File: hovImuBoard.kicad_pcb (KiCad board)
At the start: 2 copper layers, 71 x 60 mm, 78 parts, among them J1 AVR-ISP-6, J2 Ext. Power, J3 54602-908LF, J4 AVR-JTAG-10, J5 ExtensionPort, U1 LD2981, U2 BMX160, U3 SN65HVD32DR, U4 ATmega1284P-AU, U5 TPS62173DSG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

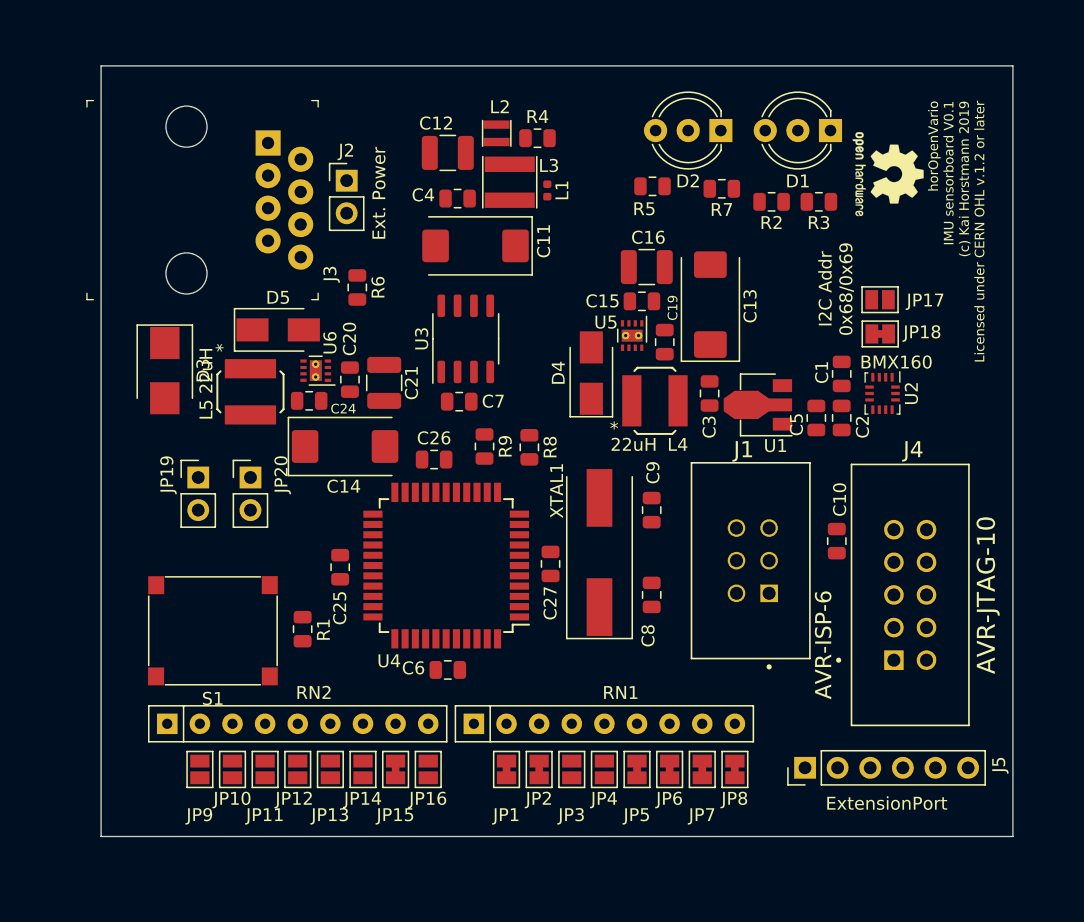
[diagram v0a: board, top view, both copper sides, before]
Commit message: First shot routing the board
Simplified the design: The IP address is not configurable with solder jumpers any more.
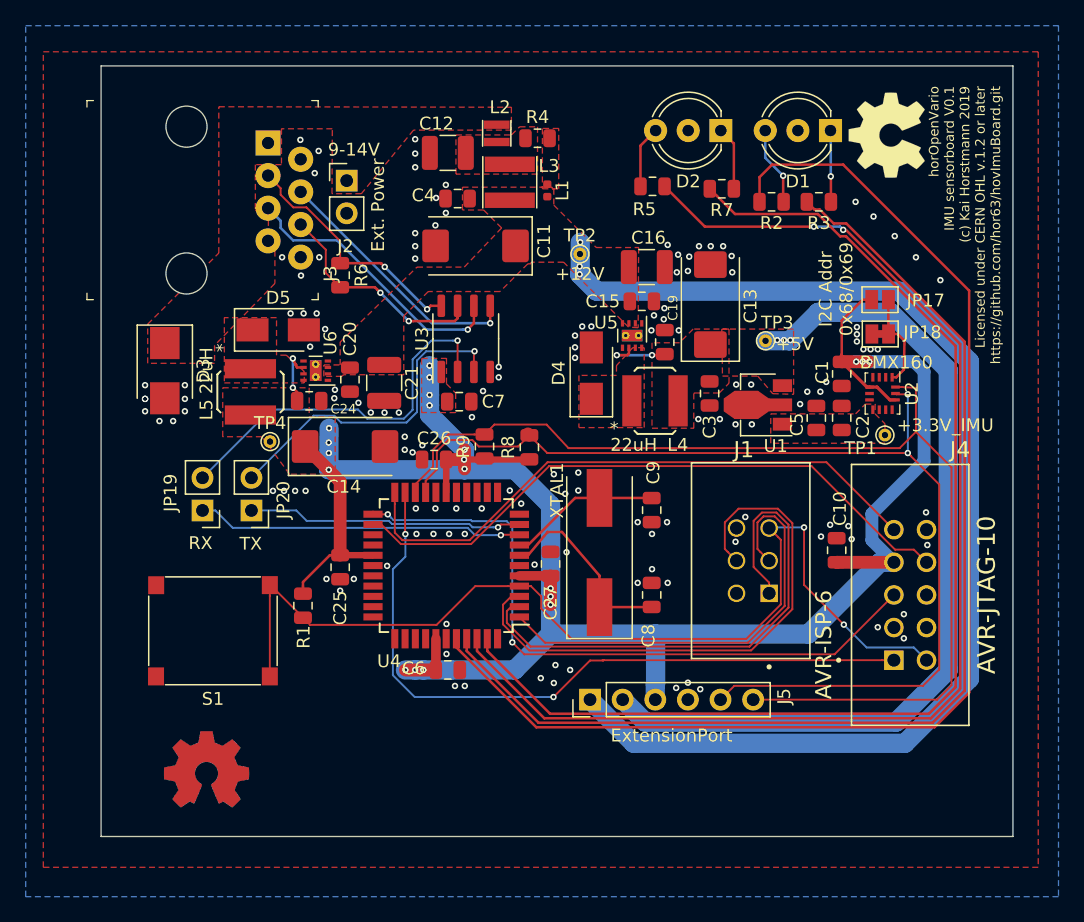
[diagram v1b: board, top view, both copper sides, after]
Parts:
- removed JP1: J15, Jumper:SolderJumper-2_P1.3mm_Bridged_Pad1.0x1.5mm
- removed JP10: J6, Jumper:SolderJumper-2_P1.3mm_Open_Pad1.0x1.5mm
- removed JP11: J5, Jumper:SolderJumper-2_P1.3mm_Open_Pad1.0x1.5mm
- removed JP12: J4, Jumper:SolderJumper-2_P1.3mm_Open_Pad1.0x1.5mm
- removed JP13: J3, Jumper:SolderJumper-2_P1.3mm_Open_Pad1.0x1.5mm
- removed JP14: J2, Jumper:SolderJumper-2_P1.3mm_Open_Pad1.0x1.5mm
- removed JP15: J1, Jumper:SolderJumper-2_P1.3mm_Bridged_Pad1.0x1.5mm
- removed JP16: J0, Jumper:SolderJumper-2_P1.3mm_Open_Pad1.0x1.5mm
- removed JP2: J14, Jumper:SolderJumper-2_P1.3mm_Bridged_Pad1.0x1.5mm
- removed JP3: J13, Jumper:SolderJumper-2_P1.3mm_Open_Pad1.0x1.5mm
- removed JP4: J12, Jumper:SolderJumper-2_P1.3mm_Open_Pad1.0x1.5mm
- removed JP5: J11, Jumper:SolderJumper-2_P1.3mm_Bridged_Pad1.0x1.5mm
- removed JP6: J10, Jumper:SolderJumper-2_P1.3mm_Bridged_Pad1.0x1.5mm
- removed JP7: J9, Jumper:SolderJumper-2_P1.3mm_Bridged_Pad1.0x1.5mm
- removed JP8: J8, Jumper:SolderJumper-2_P1.3mm_Bridged_Pad1.0x1.5mm
- removed JP9: J7, Jumper:SolderJumper-2_P1.3mm_Open_Pad1.0x1.5mm
- removed the REF** at (129.3, 98.4)
- removed RN1, RN2: 470K x 8, Resistor_THT:R_Array_SIP9
- added REF** (x2): OSHW-Symbol_6.7x6mm_Copper, Symbol:OSHW-Symbol_6.7x6mm_Copper, F.Cu at (76.2, 144.8)
- added REF**: OSHW-Symbol_6.7x6mm_SilkScreen, Symbol:OSHW-Symbol_6.7x6mm_SilkScreen, F.Cu at (129.2, 95.4)
- added TP1: +3.3V_IMU, TestPoint:TestPoint_THTPad_D1.0mm_Drill0.5mm, F.Cu at (129.0, 118.7)
- added TP2: +12V, TestPoint:TestPoint_THTPad_D1.0mm_Drill0.5mm, F.Cu at (105.3, 104.6)
- added TP3: +5V, TestPoint:TestPoint_THTPad_D1.0mm_Drill0.5mm, F.Cu at (119.7, 111.4)
- added TP4: +3.3V, TestPoint:TestPoint_THTPad_D1.0mm_Drill0.5mm, F.Cu at (81.2, 119.3)
- moved J5 17.6 mm to (106.1, 139.3)
- moved JP19 2.59 mm to (75.9, 124.6), turned to 180 degrees
- moved JP20 2.57 mm to (79.7, 124.6), turned to 180 degrees
- moved R1 1.83 mm to (83.7, 132.0), turned to 270 degrees
- moved R6 1.64 mm to (86.6, 106.3)
- moved C10 0.71 mm to (125.3, 127.7)
- turned R8 to 90 degrees
- turned R9 to 90 degrees
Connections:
- U4 pad 11: /IP10 -> (no net)
- U4 pad 12: /IP11 -> (no net)
- U4 pad 13: /IP12 -> (no net)
- U4 pad 14: /IP13 -> (no net)
- U4 pad 15: /IP14 -> (no net)
- U4 pad 16: /IP15 -> (no net)
- U4 pad 25: /IP8 -> (no net)
- U4 pad 26: /IP9 -> (no net)
- U4 pad 30: /IP7 -> (no net)
- U4 pad 31: /IP6 -> (no net)
- U4 pad 32: /IP5 -> (no net)
- U4 pad 33: /IP4 -> (no net)
- U4 pad 34: /IP3 -> (no net)
- U4 pad 35: /IP2 -> (no net)
- U4 pad 36: /IP1 -> (no net)
- U4 pad 37: /IP0 -> (no net)
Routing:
- net +3V3: track 0.00 -> 170.7 mm, vias 0 -> 22
- net /SIP_OK: track 0.00 -> 98.3 mm
- net /I2C_OK: track 0.00 -> 96.6 mm, vias 0 -> 2
- net +12V: track 0.00 -> 93.4 mm, vias 0 -> 3
- net /I2C_ERR: track 0.00 -> 91.1 mm
- net /SIP_ERR: track 0.00 -> 87.0 mm
- net /SDA: track 0.00 -> 86.1 mm
- net /SCL: track 0.00 -> 83.3 mm, vias 0 -> 2
- net /MCU_RESET: track 0.00 -> 78.3 mm, vias 0 -> 2
- net +5V: track 0.00 -> 73.3 mm, vias 0 -> 5
- net /JTAG_TCK: track 0.00 -> 55.6 mm, vias 0 -> 2
- net /JTAG_TDO: track 0.00 -> 52.5 mm, vias 0 -> 2
- net /JTAG_TDI: track 0.00 -> 49.4 mm
- net /JTAG_TMS: track 0.00 -> 46.9 mm
- net /ISP_SCK: track 0.00 -> 44.0 mm
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- added copper zone on F.Cu, net +12V
- added copper zone on F.Cu, net +3V3
- added copper zone on F.Cu, net +5V
- added copper zone on F.Cu, net +VDC
- added copper zone on F.Cu, net /3.3V_IMU
- added copper zone on B.Cu, net GND
- added copper zone on F.Cu, net GND
- added copper zone on F.Cu, net Net-(C12-Pad2)
- added copper zone on F.Cu, net Net-(D4-Pad1)
- added copper zone on F.Cu, net Net-(D5-Pad1)
- added copper zone on F.Cu, net Net-(L1-Pad1)
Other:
- board text added: "9-14V"
- board text added: "RX"
- board text added: "TX"
- board text added: "horOpenVario IMU sensorboard V0.1 (c) Kai Horstmann 2019 Licensed under CERN OHL v.1.2 or later https://github.com/hor63/hovImuBoard.git"
- board text removed: "horOpenVario IMU sensorboard V0.1 (c) Kai Horstmann 2019 Licensed under CERN OHL v.1.2 or later"

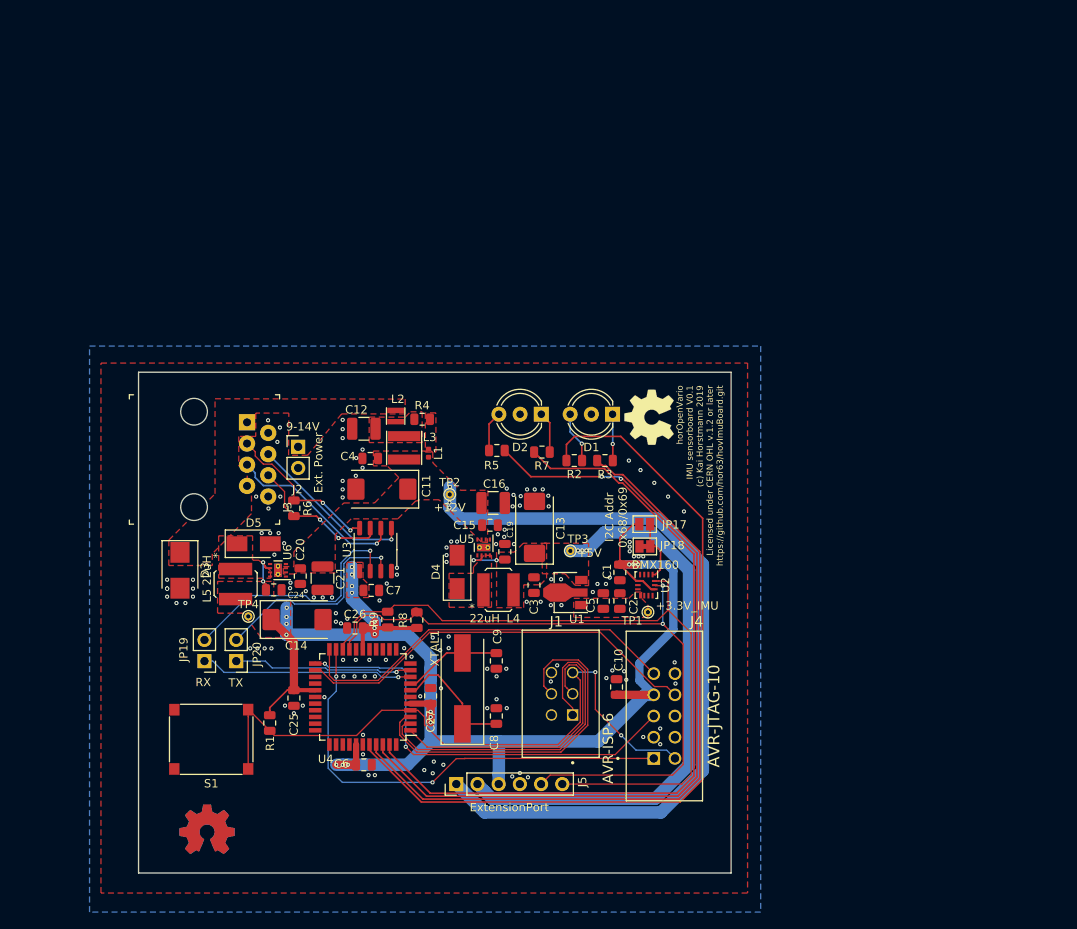
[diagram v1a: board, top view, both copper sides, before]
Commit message: Re-arrange expansion port and LEDs. Route power further apart from the BMX160 Add mounting holes.
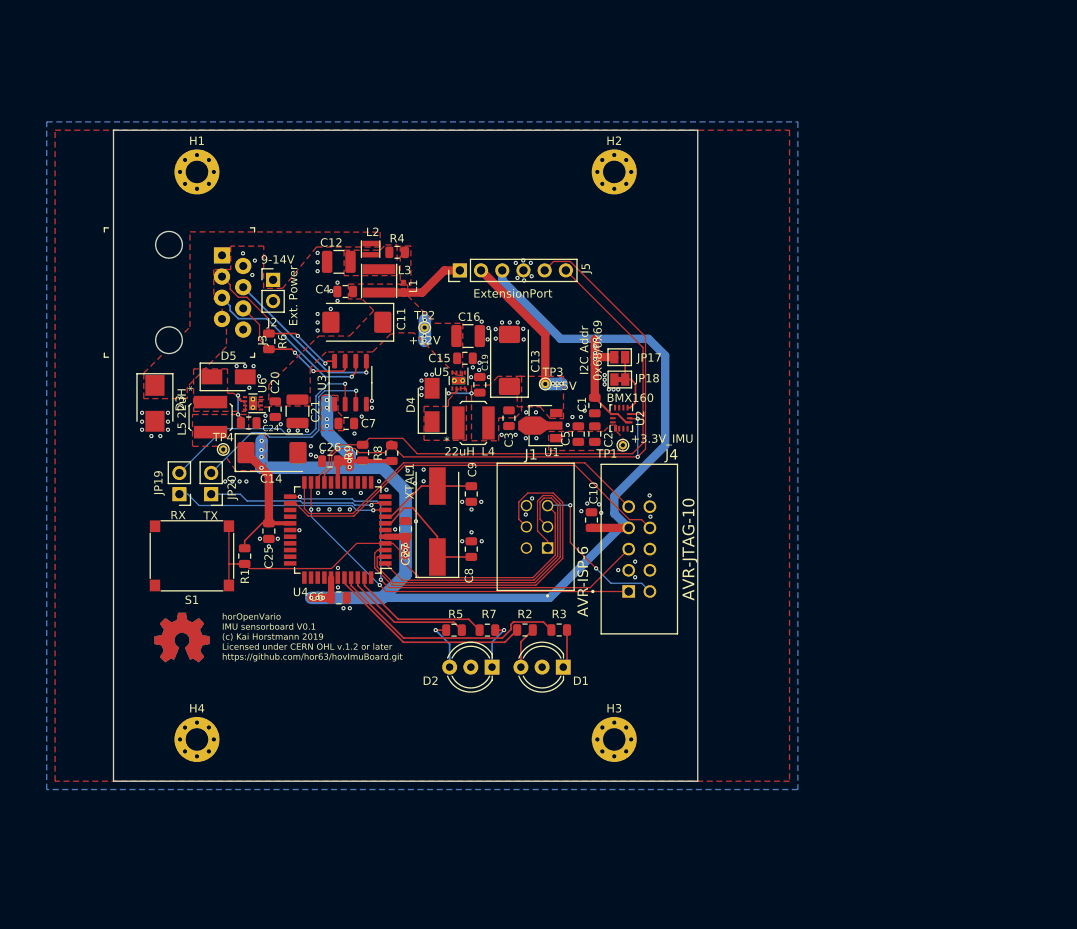
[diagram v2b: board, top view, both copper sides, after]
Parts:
- removed REF** (x2): OSHW-Symbol_6.7x6mm_Copper, Symbol:OSHW-Symbol_6.7x6mm_Copper
- removed REF**: OSHW-Symbol_6.7x6mm_SilkScreen, Symbol:OSHW-Symbol_6.7x6mm_SilkScreen
- added H1: MountingHole_Pad, MountingHole:MountingHole_2.7mm_M2.5_Pad_Via, F.Cu at (75.0, 66.0)
- added H2: MountingHole_Pad, MountingHole:MountingHole_2.7mm_M2.5_Pad_Via, F.Cu at (125.0, 66.0)
- added H3: MountingHole_Pad, MountingHole:MountingHole_2.7mm_M2.5_Pad_Via, F.Cu at (125.0, 134.0)
- added H4: MountingHole_Pad, MountingHole:MountingHole_2.7mm_M2.5_Pad_Via, F.Cu at (75.0, 134.0)
- added LOGO1, LOGO2: Logo_Open_Hardware_Small, Symbol:OSHW-Symbol_6.7x6mm_Copper, F.Cu at (73.2, 121.8)
- C8, C9: value 18pF -> 20pF
- XTAL1: value 8MHz -> 9,216MHz
- moved J5 61.5 mm to (106.5, 77.8)
- moved D1 30.9 mm to (118.9, 125.3)
- moved D2 30.9 mm to (110.4, 125.3)
- moved R7 22.3 mm to (109.8, 120.9)
- moved R5 22.1 mm to (105.8, 120.9)
- moved S1 22.1 mm to (74.4, 112.0)
- moved R2 21.1 mm to (114.3, 120.9)
- moved R3 21.0 mm to (118.4, 120.9)
- moved C25 20.2 mm to (83.6, 109.0)
- moved JP17 20.2 mm to (125.7, 88.2)
- moved TP1 20.2 mm to (126.0, 98.7)
- moved C1 20.2 mm to (122.7, 94.0)
- moved C10 20.2 mm to (122.3, 107.7)
- moved C11 20.2 mm to (94.2, 84.0)
- moved C12 20.2 mm to (92.0, 76.8)
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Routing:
- net /I2C_OK: track 96.6 -> 15.6 mm, vias 2 -> 0
- net +12V: track 93.4 -> 13.3 mm
- net /I2C_ERR: track 91.1 -> 17.0 mm
- net /SIP_OK: track 98.3 -> 24.9 mm
- net /SIP_ERR: track 87.0 -> 29.1 mm
- net +5V: track 73.3 -> 24.0 mm
- net +3V3: track 170.7 -> 198.1 mm, vias 22 -> 23
- net /SDA: track 86.1 -> 70.4 mm
- net /JTAG_TCK: track 55.6 -> 45.9 mm
- net /SCL: track 83.3 -> 78.5 mm
- net /MCU_RESET: track 78.3 -> 76.6 mm
- net Net-(D2-Pad3): track 4.83 -> 6.39 mm, vias 0 -> 1
- net Net-(D2-Pad1): track 4.96 -> 6.09 mm, vias 0 -> 1
- net Net-(D1-Pad3): track 6.14 -> 5.04 mm, vias 1 -> 0
- net Net-(D1-Pad1): track 5.56 -> 4.63 mm, vias 1 -> 0
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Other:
- board size 71 x 60 mm -> 70 x 78 mm

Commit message: Apply corrections from V0.1; Fit board to a plastic box
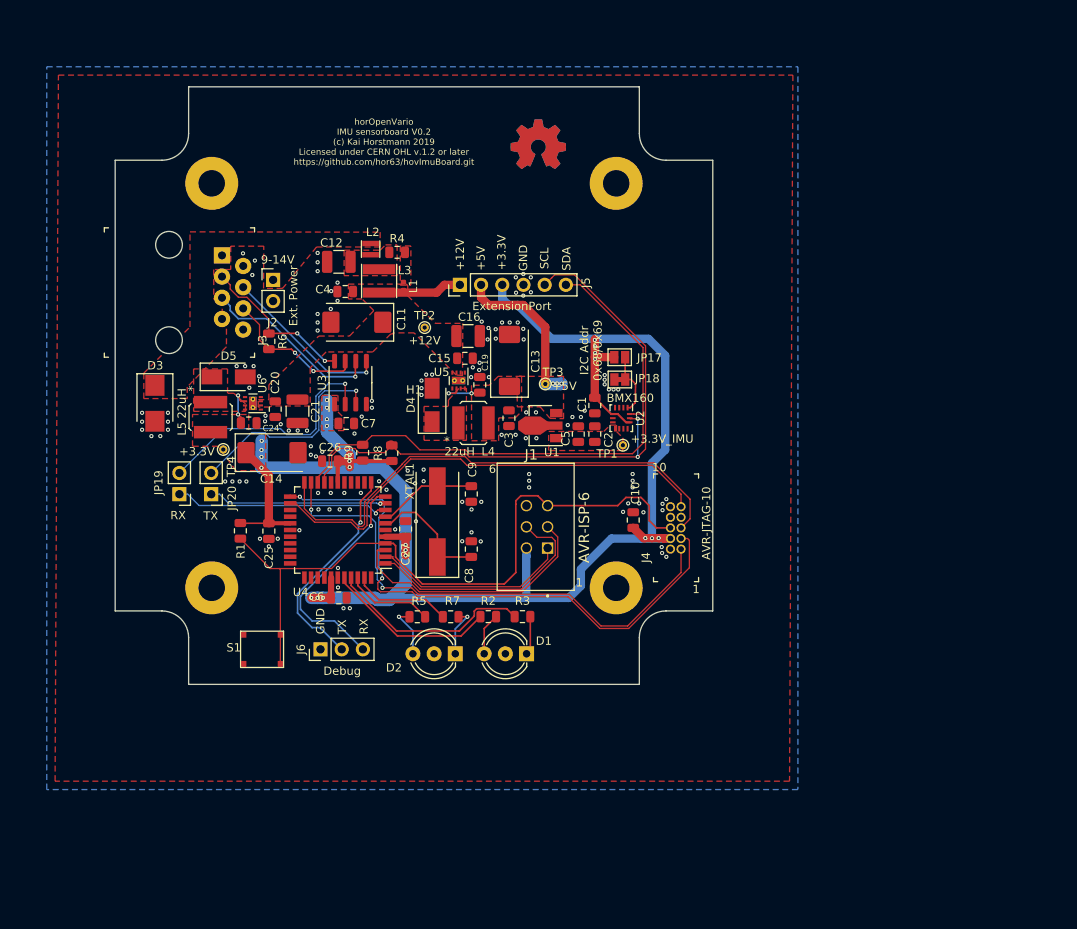
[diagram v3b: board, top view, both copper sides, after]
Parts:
- removed H2, H3, H4: MountingHole_Pad, MountingHole:MountingHole_2.7mm_M2.5_Pad_Via
- added J6: Debug, Connector_PinHeader_2.54mm:PinHeader_1x03_P2.54mm_Vertical, F.Cu at (89.8, 123.2)
- H1: value MountingHole_Pad -> Box; footprint MountingHole:MountingHole_2.7mm_M2.5_Pad_Via -> hovImuBoard:Box-CU-1935-MB
- J4: footprint hovImuBoard:TE_5104338-1 -> digikey-footprints:PinHeader_2x5_P1.27mm_Drill.7mm
- JP17: value I2C1 -> 0x69
- JP18: value I2C0 -> 0x68
- R2, R3, R5, R7: value 155 -> 200
- moved LOGO1 72.9 mm to (115.9, 62.7)
- moved LOGO2 72.9 mm to (115.9, 62.7)
- moved H1 36.5 mm to (101.0, 91.6)
- moved S1 14.0 mm to (82.8, 123.2)
- moved C10 5.00 mm to (127.3, 107.7)
- moved J4 5.00 mm to (133.0, 111.2)
- moved D1 4.68 mm to (114.5, 123.7)
- moved D2 4.68 mm to (106.0, 123.7)
- moved R3 4.68 mm to (114.0, 119.3)
- moved R5 4.68 mm to (101.4, 119.3)
- moved R7 4.68 mm to (105.4, 119.3)
- moved R2 4.68 mm to (109.9, 119.3)
- moved R1 3.07 mm to (80.2, 109.0)
- moved J5 1.73 mm to (106.5, 79.5)
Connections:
- J1 pad 2: (no net) -> +3V3
- J1 pad 3: /ISP_MOSI -> /ISP_SCK
- J1 pad 4: /ISP_SCK -> /ISP_MOSI
- U4 pad 11: (no net) -> /RX_DBG
- U4 pad 12: (no net) -> /TX_DBG
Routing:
- net /RX_DBG: track 0.00 -> 27.7 mm, vias 0 -> 1
- net /TX_DBG: track 0.00 -> 26.4 mm, vias 0 -> 1
- net /ISP_MISO: track 42.1 -> 23.8 mm
- net /JTAG_TCK: track 45.9 -> 63.3 mm
- net /JTAG_TDO: track 52.5 -> 69.5 mm
- net /JTAG_TMS: track 46.9 -> 61.3 mm
- net /ISP_SCK: track 44.1 -> 31.7 mm
- net +3V3: track 198.1 -> 207.4 mm, vias 23 -> 26
- net /JTAG_TDI: track 49.4 -> 56.4 mm
- net /ISP_MOSI: track 34.9 -> 29.2 mm
- net /I2C_ERR: track 17.0 -> 11.9 mm
- net /I2C_OK: track 15.6 -> 10.6 mm
- net /MCU_RESET: track 76.6 -> 81.5 mm, vias 2 -> 0
- net /SIP_ERR: track 29.1 -> 24.6 mm
- net /SIP_OK: track 24.9 -> 20.5 mm
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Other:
- board size 70 x 78 mm -> 71.6 x 71.6 mm
- board text added: "+12V"
- board text added: "+3.3V"
- board text added: "+5V"
- board text added: "1"
- board text added: "10"
- board text added: "6"
- board text added: "GND"
- board text added: "SCL"
- board text added: "SDA"
- board text added: "horOpenVario IMU sensorboard V0.2 (c) Kai Horstmann 2019 Licensed under CERN OHL v.1.2 or later https://github.com/hor63/hovImuBoard.git"
- board text removed: "horOpenVario IMU sensorboard V0.1 (c) Kai Horstmann 2019 Licensed under CERN OHL v.1.2 or later https://github.com/hor63/hovImuBoard.git"
